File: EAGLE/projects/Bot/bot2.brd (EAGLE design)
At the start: 122.5 x 95 mm, 22 parts, among them IC1 7805T, U3 ARDUINO_SHIELDLABEL

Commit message: PCB Updates
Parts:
- IC1: value 7805T -> (none); device linear:TO220H -> linearMe:TO220H
- LED1, LED2, LED3: device led:LED5MM -> ledMe:LED5MM
- S2: device switch1:MS243 -> switch2:MS243
- U$1, U$2: value ULTRASONIC-HC-SR04#V -> ULTRASONIC-HC-SR04; device diy-modules:ULTRASONIC-HC-SR04#V -> diy-modules:ULTRASONIC-HC-SR04
- moved S2 6.88 mm to (113.0, 77.5), turned to 180 degrees
- moved U$1 1.40 mm to (103.4, 12.3)
- moved U$2 1.28 mm to (65.9, 12.0)
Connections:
- net 0: now also IC1.1; no longer IC1.2
- net PI_5V: now also LED1.A, LED2.A
- net PWR+: now also IC1.2; no longer IC1.1, LED1.A, LED2.A
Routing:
- net PWR+: track 233.2 -> 192.1 mm
- net PI_3V3: track 120.1 -> 82.3 mm
- net 0: track 470.0 -> 462.0 mm
- net N$7: track 0.00 -> 7.20 mm
- net PI_5V: track 317.0 -> 321.7 mm
- net R_FWD: track 162.4 -> 165.1 mm
- net N$13: track 35.4 -> 36.3 mm
- net N$15: track 47.2 -> 47.8 mm
- net R_SPD: track 91.6 -> 92.2 mm

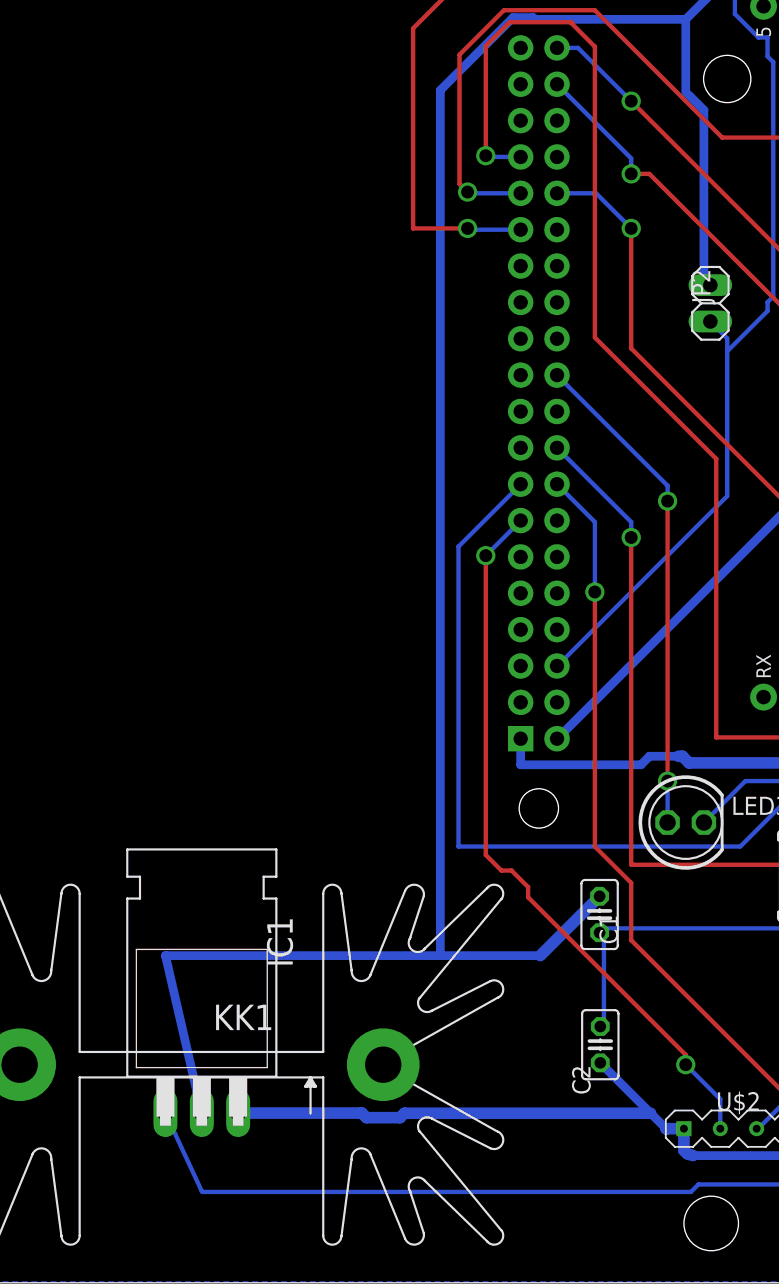
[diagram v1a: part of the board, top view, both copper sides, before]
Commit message: Fixed voltage reg on Eagle
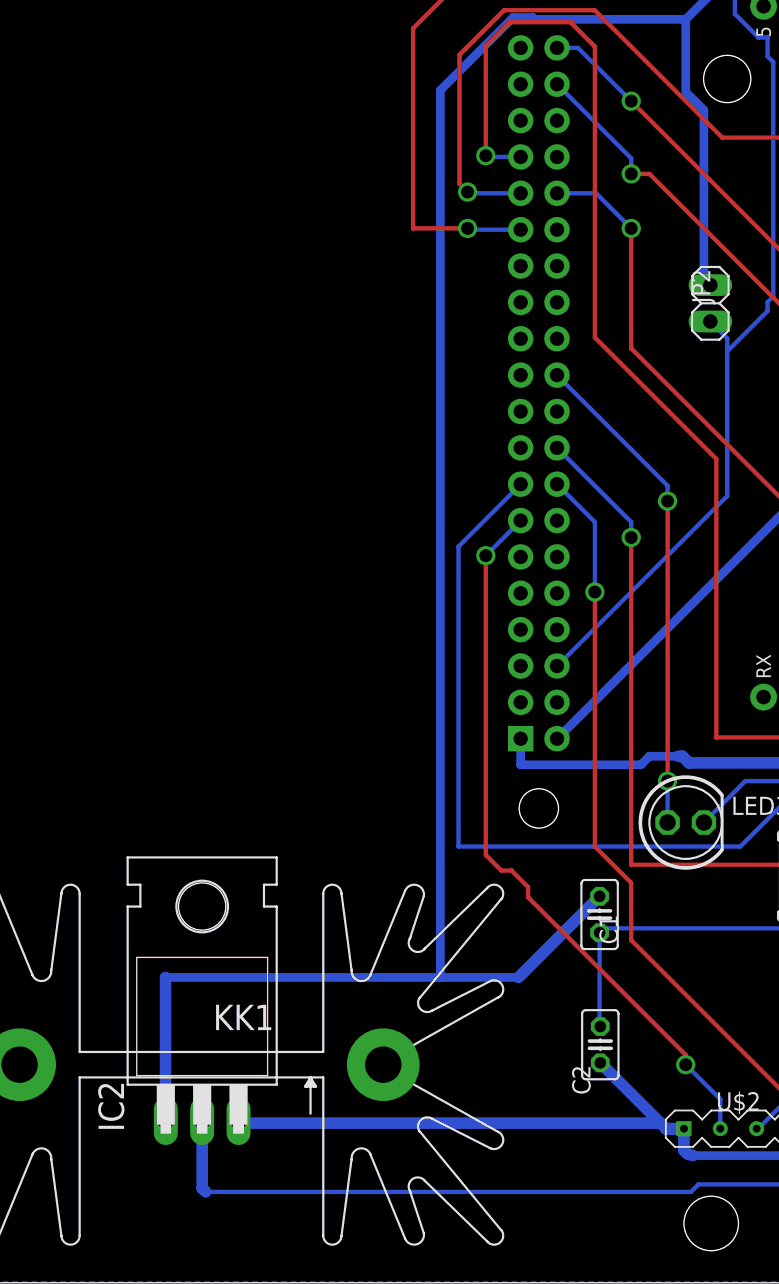
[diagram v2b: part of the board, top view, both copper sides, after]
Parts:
- removed IC1: (no value), linearMe:TO220H
- added IC2: 7805T, linear:TO220H
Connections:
- net 0: now also IC2.2; no longer IC1.1
- net PI_5V: now also IC2.3; no longer IC1.3
- net PWR+: now also IC2.1; no longer IC1.2
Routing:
- net PI_5V: track 321.7 -> 323.9 mm
- net 0: track 462.0 -> 460.9 mm
- net PWR+: track 192.1 -> 193.1 mm
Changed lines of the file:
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@@
 <attribute name="VALUE" x="55.1942" y="15.3924" size="1.27" layer="27" ratio="10" rot="R90"/>
-</element>
-<element name="IC1" library="linearMe" package="TO220H" package3d_urn="urn:adsk.eagle:package:16414/1" value="" x="28.4226" y="22.0218" smashed="yes">
-<attribute name="NAME" x="34.7726" y="22.0218" size="1.778" layer="25" ratio="10" rot="R90"/>
-<attribute name="POPULARITY" value="0" x="28.4226" y="22.0218" size="1.778" layer="27" display="off"/>
-<attribute name="VALUE" x="23.3426" y="24.5618" size="1.778" layer="27" ratio="10" rot="R90"/>
 </element>
 <element name="JP2" library="pinhead" library_urn="urn:adsk.eagle:library:325" package="1X02" package3d_urn="urn:adsk.eagle:package:22435/2" value="" x="63.948453125" y="68.4276" smashed="yes" rot="R90">
@@
 <attribute name="VALUE" x="108.5088" y="81.3308" size="1.778" layer="27" ratio="10" rot="R180"/>
 </element>
+<element name="IC2" library="linear" library_urn="urn:adsk.eagle:library:262" package="TO220H" package3d_urn="urn:adsk.eagle:package:16414/1" value="7805T" x="28.448" y="21.463" smashed="yes">
+<attribute name="NAME" x="22.987" y="10.541" size="1.778" layer="25" ratio="10" rot="R90"/>
+<attribute name="POPULARITY" value="35" x="28.448" y="21.463" size="1.778" layer="27" display="off"/>
+<attribute name="VALUE" x="35.814" y="10.414" size="1.778" layer="27" ratio="10" rot="R90"/>
+</element>
 </elements>
 <signals>
 <signal name="PWR+">
-<contactref element="IC1" pad="2"/>
 <contactref element="JP2" pad="2"/>
 <contactref element="C1" pad="1"/>
@@
 <wire x1="51.562" y1="88.392" x2="50.165" y2="88.392" width="0.6096" layer="16"/>
 <wire x1="50.165" y1="88.392" x2="45.085" y2="83.312" width="0.6096" layer="16"/>
-<wire x1="45.085" y1="83.312" x2="45.085" y2="22.86" width="0.6096" layer="16"/>
-<wire x1="25.8826" y1="22.86" x2="45.085" y2="22.86" width="0.6096" layer="16"/>
-<wire x1="25.8826" y1="22.86" x2="28.4226" y2="11.8618" width="0.6096" layer="16"/>
-<wire x1="45.085" y1="22.86" x2="52.07" y2="22.86" width="0.6096" layer="16"/>
+<wire x1="45.085" y1="83.312" x2="45.085" y2="21.336" width="0.6096" layer="16"/>
+<wire x1="25.8826" y1="21.336" x2="45.085" y2="21.336" width="0.6096" layer="16"/>
+<wire x1="45.085" y1="21.336" x2="50.546" y2="21.336" width="0.6096" layer="16"/>
 <wire x1="64.0414" y1="91.0490875" x2="65.5673125" y2="92.575" width="0.6096" layer="16"/>
 <wire x1="62.23" y1="88.265" x2="64.0414" y2="90.0764" width="0.6096" layer="16"/>
@@
 <wire x1="105.029" y1="85.6234" x2="104.9528" y2="85.5472" width="0.6096" layer="16"/>
 <wire x1="65.5673125" y1="92.575" x2="100.8714" y2="92.575" width="0.6096" layer="16"/>
-<wire x1="52.07" y1="22.86" x2="56.2102" y2="27.0002" width="0.8128" layer="16"/>
+<wire x1="50.546" y1="21.336" x2="56.2102" y2="27.0002" width="0.8128" layer="16"/>
+<contactref element="IC2" pad="1"/>
+<wire x1="25.8826" y1="21.336" x2="25.8826" y2="11.3284" width="0.8128" layer="16"/>
+<wire x1="25.8826" y1="11.3284" x2="25.908" y2="11.303" width="0.8128" layer="16"/>
 </signal>
 <signal name="0">
-<contactref element="IC1" pad="1"/>
 <contactref element="C1" pad="2"/>
-<contactref element="C2" pad="2"/>
 <contactref element="PI" pad="6"/>
 <contactref element="R3" pad="2"/>
@@
 <contactref element="U3" pad="GND@0"/>
 <contactref element="TXS0108E1:JP2" pad="1"/>
-<wire x1="56.515" y1="24.13" x2="56.515" y2="18.415" width="0.3048" layer="16"/>
-<wire x1="56.515" y1="18.415" x2="56.261" y2="17.907" width="0.3048" layer="16"/>
-<wire x1="56.515" y1="24.13" x2="56.2102" y2="24.4602" width="0.3048" layer="16"/>
 <wire x1="71.755" y1="12.7" x2="69.84935" y2="10.79435" width="0.3048" layer="16"/>
 <wire x1="71.755" y1="23.495" x2="71.755" y2="12.7" width="0.3048" layer="16"/>
@@
 <wire x1="73.406" y1="25.146" x2="85.5472" y2="25.146" width="0.3048" layer="16"/>
 <wire x1="85.5472" y1="25.146" x2="87.5792" y2="23.114" width="0.3048" layer="16"/>
-<wire x1="28.4734" y1="6.35" x2="62.59261875" y2="6.35" width="0.3048" layer="16"/>
+<wire x1="28.4734" y1="6.35" x2="28.702" y2="6.35" width="0.3048" layer="16"/>
+<wire x1="28.702" y1="6.35" x2="62.59261875" y2="6.35" width="0.3048" layer="16"/>
 <wire x1="108.3907375" y1="6.7907375" x2="110.49" y2="8.89" width="0.3048" layer="16"/>
 <wire x1="104.9856875" y1="6.7907375" x2="108.3907375" y2="6.7907375" width="0.3048" layer="16"/>
@@
 <wire x1="63.118025" y1="6.87540625" x2="98.6605375" y2="6.87540625" width="0.3048" layer="16"/>
 <wire x1="98.6605375" y1="6.87540625" x2="99.34334375" y2="6.1926" width="0.3048" layer="16"/>
-<wire x1="25.8826" y1="11.8618" x2="28.4226" y2="6.4008" width="0.3048" layer="16"/>
 <wire x1="28.4226" y1="6.4008" x2="28.4734" y2="6.35" width="0.3048" layer="16"/>
 <wire x1="112.9538" y1="75.4888" x2="112.9538" y2="75.0824" width="0.8128" layer="16"/>
 <wire x1="112.9538" y1="75.0824" x2="112.903" y2="75.0316" width="0.8128" layer="16"/>
-<wire x1="100.8126" y1="70.993" x2="112.9538" y2="75.4888" width="0" layer="19" extent="1-1"/>
+<contactref element="IC2" pad="2"/>
+<contactref element="C2" pad="2"/>
+<wire x1="28.702" y1="6.35" x2="28.448" y2="6.604" width="0.8128" layer="16"/>
+<wire x1="28.448" y1="6.604" x2="28.448" y2="11.303" width="0.8128" layer="16"/>
+<wire x1="56.2102" y1="24.4602" x2="56.2102" y2="17.9578" width="0.3048" layer="16"/>
+<wire x1="56.2102" y1="17.9578" x2="56.261" y2="17.907" width="0.3048" layer="16"/>
 </signal>
 <signal name="L_FWD">
@@
 <contactref element="U3" pad="A1"/>
 <contactref element="U3" pad="5V"/>
-<contactref element="IC1" pad="3"/>
 <contactref element="C2" pad="1"/>
 <contactref element="TXS0108E1:JP2" pad="10"/>
@@
 <wire x1="78.105" y1="86.995" x2="90.805" y2="86.995" width="0.3048" layer="16"/>
 <wire x1="99.695" y1="32.385" x2="99.822" y2="32.385" width="0.3048" layer="16"/>
-<wire x1="56.261" y1="15.367" x2="59.7789" y2="11.8491" width="0.6096" layer="16"/>
-<wire x1="59.7789" y1="11.8491" x2="60.833" y2="10.795" width="0.6096" layer="16"/>
+<wire x1="60.4694" y1="11.1586" x2="60.833" y2="10.795" width="0.6096" layer="16"/>
 <wire x1="93.69515625" y1="8.89" x2="99.568" y2="10.9982" width="0.6096" layer="16"/>
 <wire x1="62.7337625" y1="8.89" x2="87.757" y2="8.89" width="0.6096" layer="16"/>
@@
 <wire x1="62.103" y1="10.7696" x2="62.103" y2="9.2456" width="0.8128" layer="16"/>
 <wire x1="62.7337625" y1="8.89" x2="62.326521875" y2="9.022078125" width="0.8128" layer="16"/>
-<wire x1="30.9626" y1="11.8618" x2="39.60145" y2="11.8618" width="0.8128" layer="16"/>
-<wire x1="39.60145" y1="11.8618" x2="39.92365" y2="11.5396" width="0.8128" layer="16"/>
-<wire x1="39.92365" y1="11.5396" x2="42.27075" y2="11.5396" width="0.8128" layer="16"/>
-<wire x1="42.27075" y1="11.5396" x2="42.58025" y2="11.8491" width="0.8128" layer="16"/>
-<wire x1="42.58025" y1="11.8491" x2="59.7789" y2="11.8491" width="0.8128" layer="16"/>
+<wire x1="31.1324" y1="11.1586" x2="60.4694" y2="11.1586" width="0.8128" layer="16"/>
 <wire x1="53.2366" y1="38.0118" x2="53.2518" y2="38.0118" width="0.6096" layer="16"/>
 <wire x1="53.2518" y1="38.0118" x2="70.6628" y2="55.4228" width="0.6096" layer="16"/>
@@
 <wire x1="79.1972" y1="11.43" x2="77.4446" y2="13.1826" width="0.8128" layer="16"/>
 <wire x1="79.1972" y1="11.43" x2="87.7824" y2="11.43" width="0.8128" layer="16"/>
+<contactref element="IC2" pad="3"/>
+<wire x1="30.988" y1="11.303" x2="31.1324" y2="11.1586" width="0.8128" layer="16"/>
+<wire x1="56.261" y1="15.367" x2="60.8584" y2="10.7696" width="0.8128" layer="16"/>
+<wire x1="60.8584" y1="10.7696" x2="62.103" y2="10.7696" width="0.8128" layer="16"/>
 </signal>
 <signal name="N$1">
@@
 <mfgpreviewcolor name="substratecolor" color="0xFF786E46"/>
 </mfgpreviewcolors>
-<errors>
-</errors>
 </board>
 </drawing>
